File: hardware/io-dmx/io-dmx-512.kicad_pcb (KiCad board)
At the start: 2 copper layers, 60 x 60 mm, 29 parts, among them J1 IO EXTENSION, J2 NC3FAH/NC5FAH, J3 NC3MAH/NC5MAH, U1 NMA0505SC, U2 6N137, U3 6N137, U4 6N137, U5 MAX3485CPA+

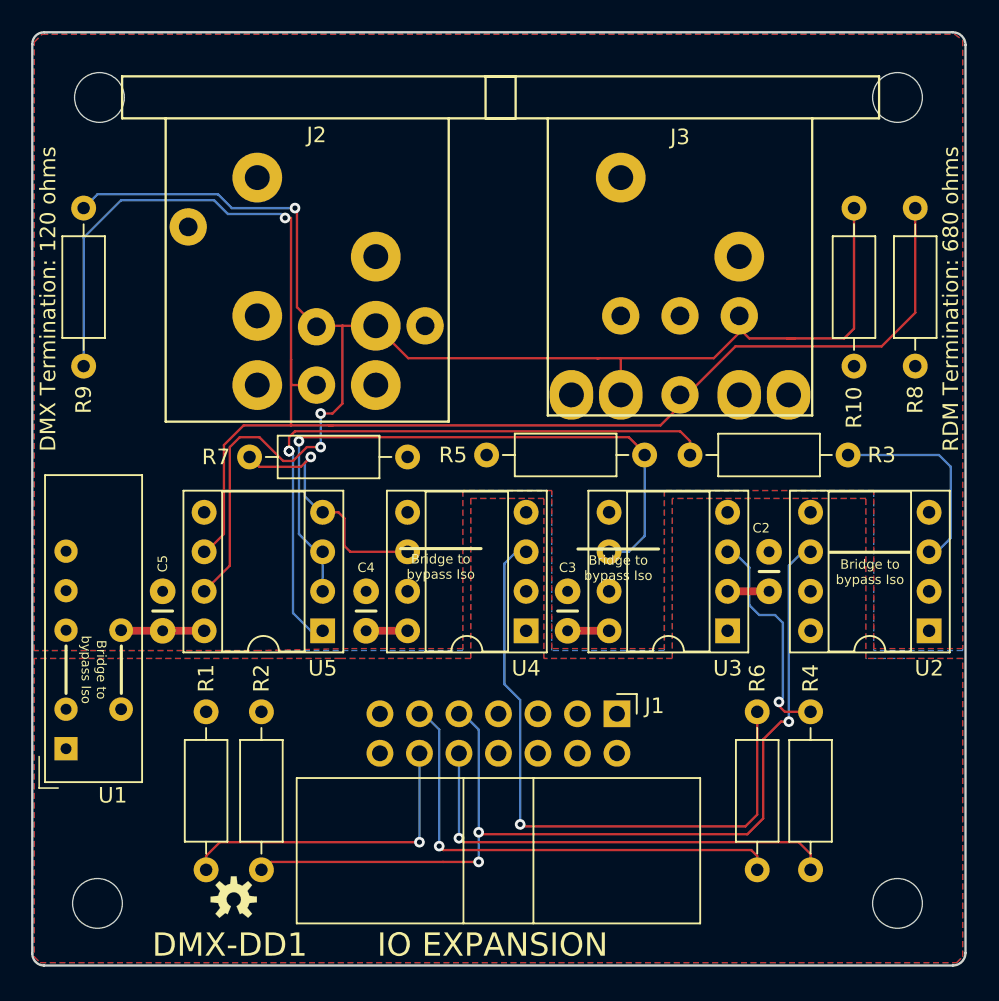
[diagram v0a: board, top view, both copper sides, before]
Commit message: Prototype version of DMX, Analog, and PWM IO Modules and both TX and RX IO interfaces.
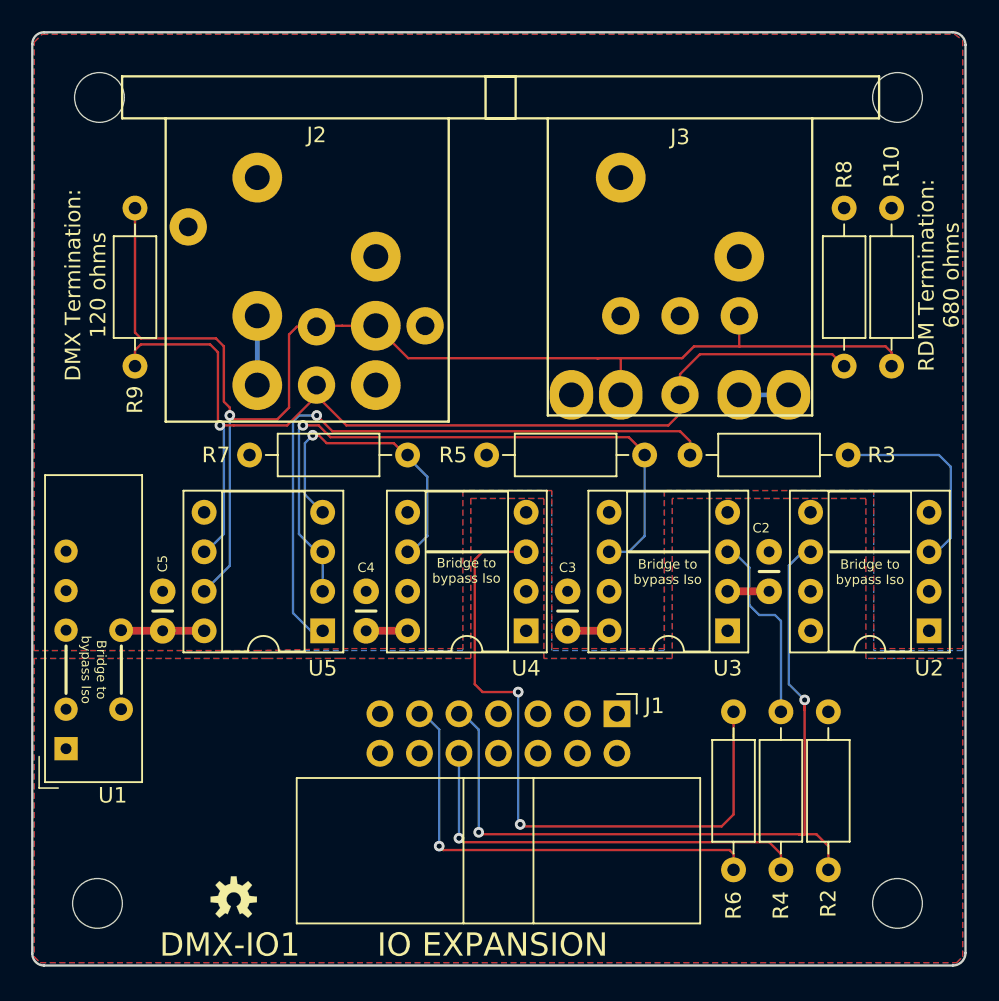
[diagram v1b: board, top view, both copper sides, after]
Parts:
- removed the ? at (154.8, 117.1)
- removed R1: 330, Resistor_THT:R_Axial_DIN0207_L6.3mm_D2.5mm_P10.16mm_Horizontal
- moved R2 36.4 mm to (165.6, 104.3)
- moved R8 11.1 mm to (166.6, 82.0), turned to 90 degrees
- moved R10 10.4 mm to (169.7, 82.0), turned to 90 degrees
- moved R7 10.2 mm to (138.6, 87.8), turned to 180 degrees
- moved R9 3.30 mm to (121.0, 71.9)
- moved R4 1.91 mm to (162.6, 104.3)
- moved R6 1.52 mm to (159.5, 104.3)
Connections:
- net Net-(J1-Pad10) renamed /DMX-DIR
- net Net-(J1-Pad11) renamed /DMX-TX
- net Net-(J1-Pad9) renamed /DMX-RX
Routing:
- net Net-(J2-Pad3): track 102.5 -> 67.1 mm
- net Net-(J1-Pad12): track 20.7 -> 0.00 mm, vias 1 -> 0
- net Net-(J2-Pad2A): track 98.7 -> 87.4 mm, vias 3 -> 1
- net /DMX-RX: track 62.1 -> 53.0 mm, vias 3 -> 2
- net GNDD: track 0.00 -> 7.62 mm
- net Net-(R7-Pad1): track 16.3 -> 19.7 mm
- net Net-(R6-Pad1): track 41.1 -> 43.8 mm, vias 1 -> 2
- net Net-(R4-Pad1): track 14.5 -> 12.5 mm, vias 1 -> 0
- net /DMX-DIR: track 29.5 -> 27.6 mm
- net /DMX-TX: track 30.8 -> 29.3 mm
- net Net-(R3-Pad1): track 40.9 -> 42.0 mm, vias 2 -> 1
- net Net-(R5-Pad1): track 41.3 -> 42.4 mm
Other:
- board text added: "DMX-IO1"
- board text added: "DMX-IO1, Rev 1.1 Crazy Giraffe Software"
- board text removed: "DMX-DD1"
- board text removed: "DMX-DD1, Rev 1.1 Crazy Giraffe Software"

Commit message: Finalize io-dmx board
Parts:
- C2, C3, C4, C5: footprint Capacitors:CAP-PTH-2.54 -> Capacitor_THT:C_Rect_L4.6mm_W2.0mm_P2.50mm_MKS02_FKP02
- moved C4 1.27 mm to (135.8, 99.1)
- moved C2 1.27 mm to (161.8, 96.5)
- moved C3 1.27 mm to (148.8, 99.1)
- moved C5 1.27 mm to (122.8, 99.1)

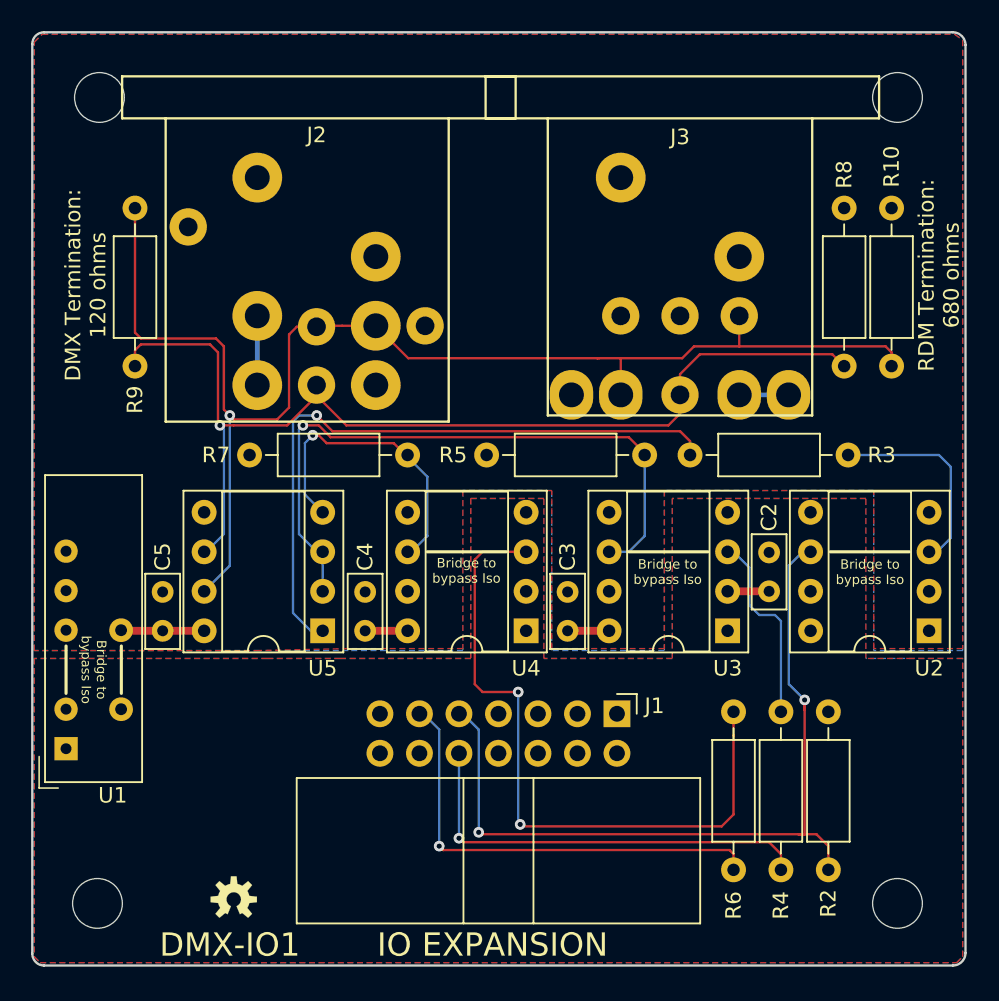
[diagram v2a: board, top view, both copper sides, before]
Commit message: Added Bill Of Materials (BOM)
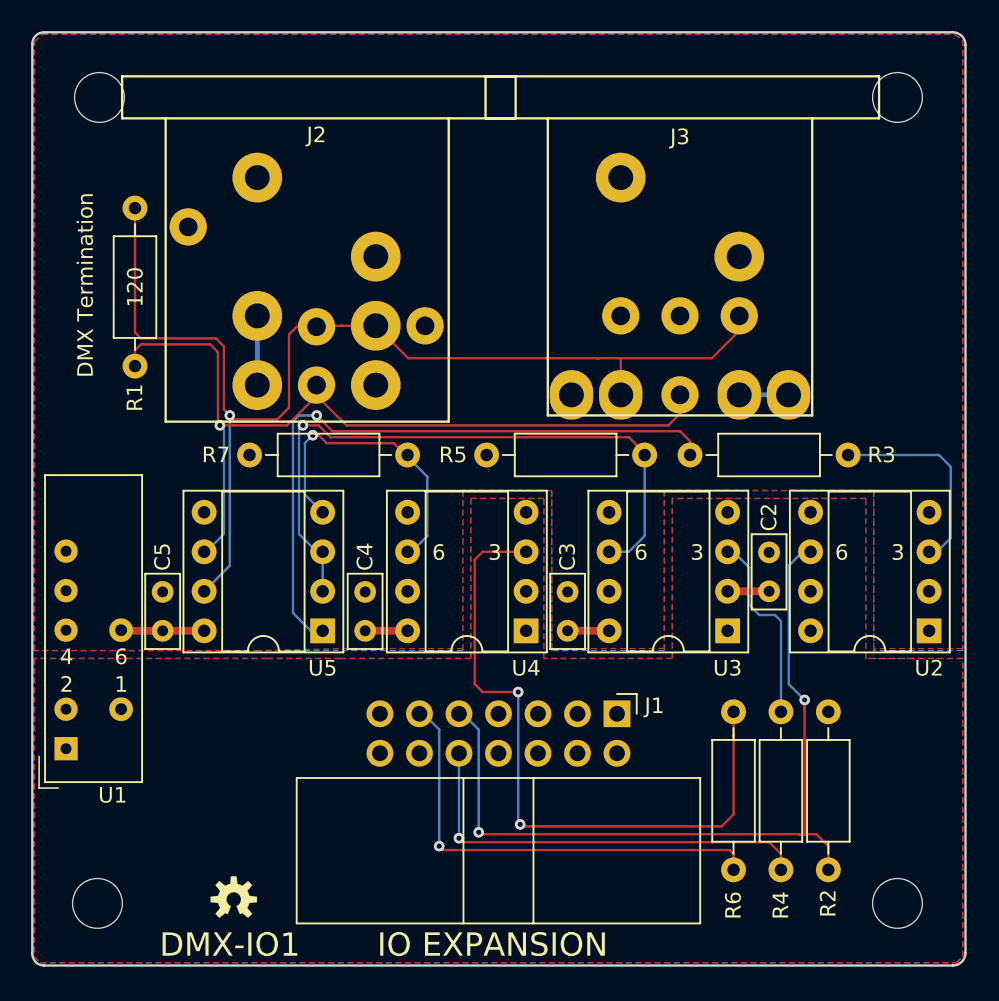
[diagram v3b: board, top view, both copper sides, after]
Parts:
- removed R10, R8: 680, Resistor_THT:R_Axial_DIN0207_L6.3mm_D2.5mm_P10.16mm_Horizontal
- removed R9: 120, Resistor_THT:R_Axial_DIN0207_L6.3mm_D2.5mm_P10.16mm_Horizontal
- added R1: 120, Resistor_THT:R_Axial_DIN0207_L6.3mm_D2.5mm_P10.16mm_Horizontal, F.Cu at (121.0, 71.9)
- C2, C3, C4, C5: value .01uF -> 0.1uF
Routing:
- net Net-(J2-Pad3): track 67.1 -> 54.4 mm
- net Net-(J2-Pad2A): track 87.4 -> 75.9 mm
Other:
- board text added: "1"
- board text added: "120"
- board text added: "2"
- board text added: "3"
- board text added: "4"
- board text added: "6"
- board text added: "DMX Termination"
- board text added: "DMX-IO1, Rev 1.3 Crazy Giraffe Software"
- board text removed: "Bridge to bypass Iso"
- board text removed: "DMX Termination: 120 ohms"
- board text removed: "DMX-IO1, Rev 1.1 Crazy Giraffe Software"
- board text removed: "RDM Termination: 680 ohms"

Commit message: Display Pro: - Switch to smaller screw terminal connectors - Add pull-down resistors - Add silkscreen values - Remove COAX power connector...again - Add test software
Core:
- Fix issue with A03 and A02 being reversed at Analog Extensions
- Fix issue with A1 and A0 at IO Extension header
- Label D0..D7 correctly
- Swap U4 and U5 in schematic to match board layout
- Change TO-92 footprint
- Add silkscreen values
- Add test software

PWM:
- Switch to smaller screw terminal connectors
- Add silkscreen values
- Remove COAX power connector

Voltage:
- Switch to smaller screw terminal connectors
- Add silkscreen values
- Remove COAX power connector

DMX:
- Fix issue with DMX A and B being reversed
- Group bypass-only resistors together
- Add ISO bypass solder bridges
- Add silkscreen values
- Remove RDM bias resistors
- Add test software

Rx-IO:
- Fix issue with A1 and A0 at IO Extension header
- Add silkscreen values

Tx-IO:
- Switch to 74LS07 for Led driver
- Add pulldown resistor for discovery
- Add silkscreen values

Discovery:
- Make use of new Tx-IO pulldown resistor
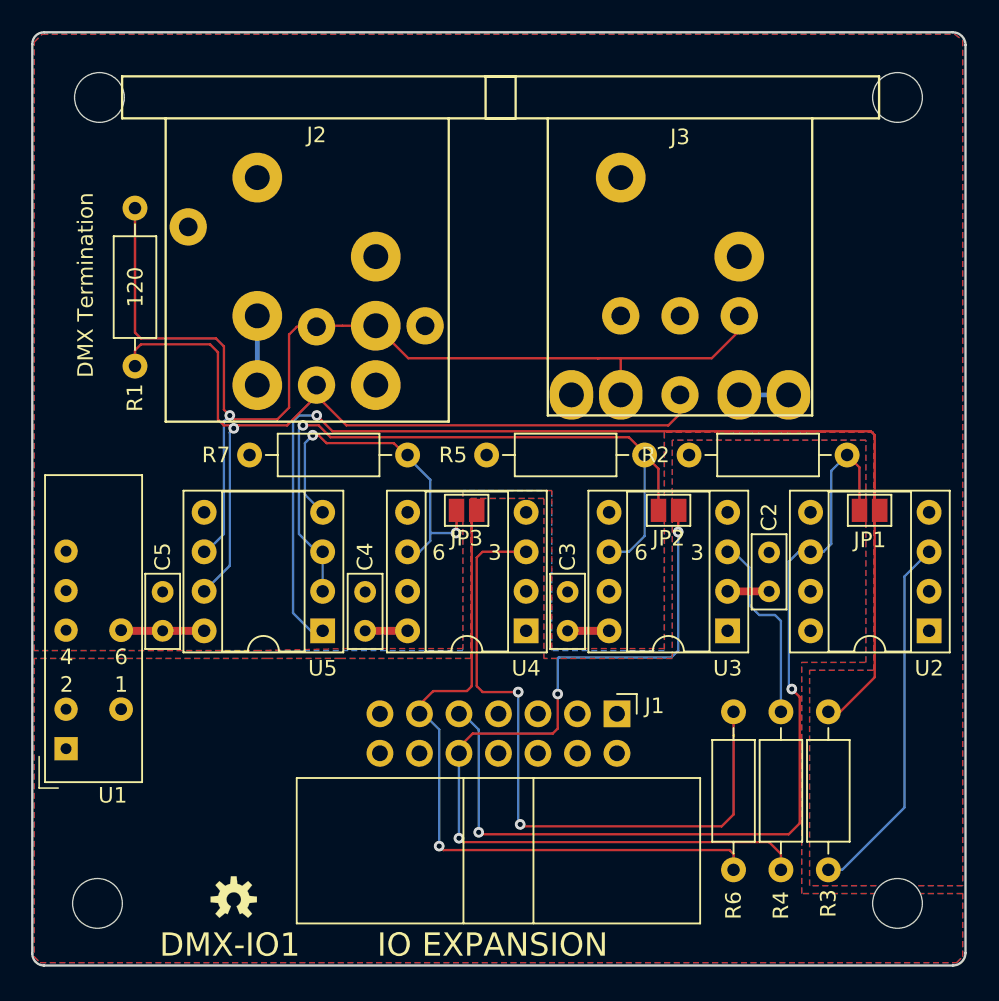
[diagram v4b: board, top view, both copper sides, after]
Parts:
- added JP1: Bypass Iso, Jumper:SolderJumper-2_P1.3mm_Open_Pad1.0x1.5mm, F.Cu at (168.3, 91.3)
- added JP2: Bypass Iso, Jumper:SolderJumper-2_P1.3mm_Open_Pad1.0x1.5mm, F.Cu at (155.3, 91.3)
- added JP3: Bypass Iso, Jumper:SolderJumper-2_P1.3mm_Open_Pad1.0x1.5mm, F.Cu at (142.4, 91.3)
- moved R2 18.8 mm to (156.7, 87.8), turned to 0 degrees
- moved R3 18.8 mm to (165.6, 104.3), turned to 270 degrees
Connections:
- U5 pad 6: Net-(J2-Pad3) -> Net-(J2-Pad2A)
- U5 pad 7: Net-(J2-Pad2A) -> Net-(J2-Pad3)
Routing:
- net Net-(JP1-Pad2): track 42.0 -> 73.3 mm
- net /DMX-DIR: track 27.6 -> 56.3 mm, vias 1 -> 3
- net /DMX-TX: track 29.3 -> 45.2 mm
- net Net-(R3-Pad2): track 13.3 -> 23.7 mm
- net /DMX-RX: track 53.0 -> 59.6 mm
- net Net-(JP2-Pad2): track 42.4 -> 46.3 mm
- net Net-(JP3-Pad2): track 19.7 -> 23.3 mm, vias 1 -> 2
- net Net-(J2-Pad3): track 54.4 -> 57.0 mm
- net Net-(J2-Pad2A): track 75.9 -> 73.5 mm
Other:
- board text added: "DMX-IO1, Rev 1.4 Crazy Giraffe Software"
- board text removed: "DMX-IO1, Rev 1.3 Crazy Giraffe Software"

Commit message: Update silk screen.
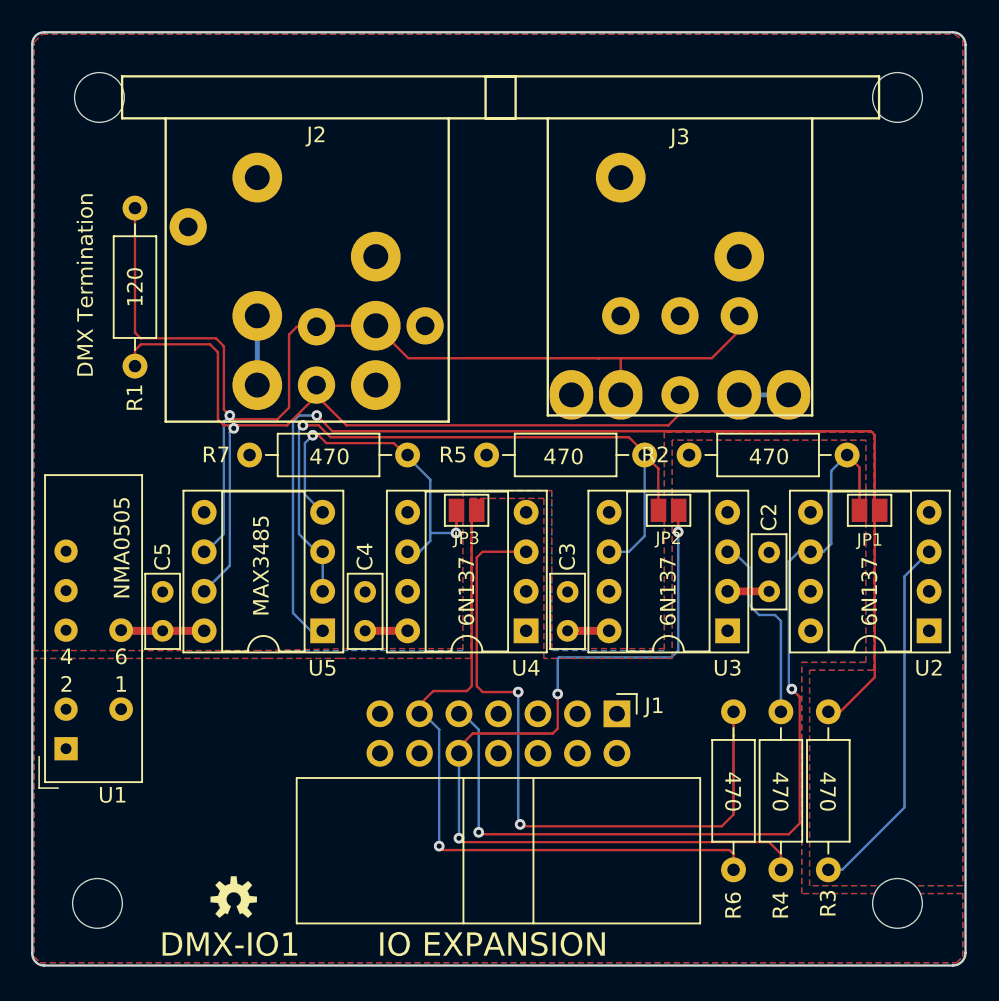
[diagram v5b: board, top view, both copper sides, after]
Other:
- board text added: "470"
- board text added: "6N137"
- board text added: "MAX3485"
- board text added: "NMA0505"
- board text removed: "3"
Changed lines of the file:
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@@
   (general
     (thickness 1.6)
-    (drawings 21)
+    (drawings 28)
     (tracks 195)
     (zones 0)
@@
     (attr virtual)
     (fp_text reference JP1 (at 0.015 1.905) (layer F.SilkS)
-      (effects (font (size 1 1) (thickness 0.15)))
+      (effects (font (size 0.8 0.8) (thickness 0.1)))
     )
     (fp_text value "Bypass Iso" (at 0 1.9) (layer F.Fab)
@@
     (attr virtual)
     (fp_text reference JP2 (at 0 -1.8 180) (layer F.SilkS)
-      (effects (font (size 1 1) (thickness 0.15)))
+      (effects (font (size 0.8 0.8) (thickness 0.1)))
     )
     (fp_text value "Bypass Iso" (at 0 1.9 180) (layer F.Fab)
@@
     (attr virtual)
     (fp_text reference JP3 (at 0 -1.8 180) (layer F.SilkS)
-      (effects (font (size 1 1) (thickness 0.15)))
+      (effects (font (size 0.8 0.8) (thickness 0.1)))
     )
     (fp_text value "Bypass Iso" (at 0 1.9 180) (layer F.Fab)
@@
     )
   )
-  (gr_text 1 (at 120.142 102.5144) (layer F.SilkS)
+  (gr_text 470 (at 165.5445 109.4105 270) (layer F.SilkS)
     (effects (font (size 1 1) (thickness 0.15)))
   )
-  (gr_text 6 (at 120.142 100.7364) (layer F.SilkS)
+  (gr_text 470 (at 162.4965 109.4105 270) (layer F.SilkS)
     (effects (font (size 1 1) (thickness 0.15)))
   )
-  (gr_text 4 (at 116.6368 100.7364) (layer F.SilkS)
+  (gr_text 470 (at 159.4485 109.4105 270) (layer F.SilkS)
     (effects (font (size 1 1) (thickness 0.15)))
   )
-  (gr_text 2 (at 116.6368 102.5144) (layer F.SilkS)
+  (gr_text 470 (at 161.798 87.884) (layer F.SilkS)
     (effects (font (size 1 1) (thickness 0.15)))
   )
-  (gr_text 120 (at 121.0564 76.962 90) (layer F.SilkS)
+  (gr_text 470 (at 148.59 87.884) (layer F.SilkS)
     (effects (font (size 1 1) (thickness 0.15)))
   )
-  (gr_text 6 (at 153.5684 94.0308) (layer F.SilkS)
+  (gr_text 470 (at 133.5405 87.884) (layer F.SilkS)
     (effects (font (size 1 1) (thickness 0.15)))
   )
-  (gr_text 3 (at 157.1752 94.0308) (layer F.SilkS)
+  (gr_text NMA0505 (at 120.2055 93.726 90) (layer F.SilkS)
     (effects (font (size 1 1) (thickness 0.15)))
   )
-  (gr_text 3 (at 144.1704 94.0308) (layer F.SilkS)
+  (gr_text 6N137 (at 168.275 96.52 90) (layer F.SilkS)
     (effects (font (size 1 1) (thickness 0.15)))
   )
-  (gr_text 6 (at 140.5636 94.0308) (layer F.SilkS)
+  (gr_text 6N137 (at 155.321 96.52 90) (layer F.SilkS)
+    (effects (font (size 1 1) (thickness 0.15)))
+  )
+  (gr_text 6N137 (at 142.367 96.52 90) (layer F.SilkS)
+    (effects (font (size 1 1) (thickness 0.15)))
+  )
+  (gr_text MAX3485 (at 129.159 94.869 90) (layer F.SilkS)
+    (effects (font (size 1 1) (thickness 0.15)))
+  )
+  (gr_text 1 (at 120.142 102.5144) (layer F.SilkS)
+    (effects (font (size 1 1) (thickness 0.15)))
+  )
+  (gr_text 6 (at 120.142 100.7364) (layer F.SilkS)
+    (effects (font (size 1 1) (thickness 0.15)))
+  )
+  (gr_text 4 (at 116.6368 100.7364) (layer F.SilkS)
+    (effects (font (size 1 1) (thickness 0.15)))
+  )
+  (gr_text 2 (at 116.6368 102.5144) (layer F.SilkS)
+    (effects (font (size 1 1) (thickness 0.15)))
+  )
+  (gr_text 120 (at 121.0564 76.962 90) (layer F.SilkS)
     (effects (font (size 1 1) (thickness 0.15)))
   )
@@
   (segment (start 159.880793 78.81216) (end 159.880793 79.133207) (width 0.1524) (layer F.Cu) (net 4))
   (segment (start 159.880793 79.616793) (end 159.880793 78.81216) (width 0.1524) (layer F.Cu) (net 4))
-  (segment (start 127.127 94.869) (end 125.476 96.52) (width 0.1524) (layer B.Cu) (net 5))
   (via (at 127.127 85.217) (size 0.6858) (drill 0.3302) (layers F.Cu B.Cu) (net 4))
   (segment (start 131.43484 79.51216) (end 132.702793 79.51216) (width 0.1524) (layer F.Cu) (net 4))
@@
   (segment (start 125.603 93.98) (end 126.746 92.837) (width 0.1524) (layer B.Cu) (net 4))
   (segment (start 126.746 92.837) (end 126.746 85.598) (width 0.1524) (layer B.Cu) (net 4))
+  (segment (start 127.127 94.869) (end 125.476 96.52) (width 0.1524) (layer B.Cu) (net 5))
   (segment (start 156.070793 85.102207) (end 156.070793 83.89216) (width 0.1524) (layer F.Cu) (net 5))
   (segment (start 155.321 85.852) (end 156.070793 85.102207) (width 0.1524) (layer F.Cu) (net 5))
